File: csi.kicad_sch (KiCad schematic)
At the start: 0 parts

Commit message: finished v1
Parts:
- added J3: Conn_01x20, symbol Connector_Generic:Conn_01x20
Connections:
- new net +3.3V: J3.8 (Pin_8)
- new net CSI_DATA_2: J3.11 (Pin_11)
- new net CSI_DATA_3: J3.18 (Pin_18)
- new net CSI_DATA_4: J3.14 (Pin_14)
- new net CSI_DATA_5: J3.16 (Pin_16)
- new net CSI_DATA_6: J3.9 (Pin_9)
- new net CSI_DATA_7: J3.13 (Pin_13)
- new net CSI_DATA_8: J3.10 (Pin_10)
- new net CSI_DATA_9: J3.12 (Pin_12)
- new net CSI_HSYNC: J3.15 (Pin_15)
- new net CSI_MCLK: J3.1 (Pin_1)
- new net CSI_PIXCLK: J3.20 (Pin_20)
- new net CSI_VSYNC: J3.17 (Pin_17)
- new net GND: J3.19 (Pin_19), J3.2 (Pin_2)
- new net LDO_EN: J3.7 (Pin_7)
- new net LPI2C2_SCL: J3.4 (Pin_4)
- new net LPI2C2_SDA: J3.3 (Pin_3)
- new net PWDN: J3.6 (Pin_6)
- new net XRS: J3.5 (Pin_5)
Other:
- note added: "????"
- company: (none) -> Northeastern University
- title: (none) -> RT1050 DevBoard for Project Horizon

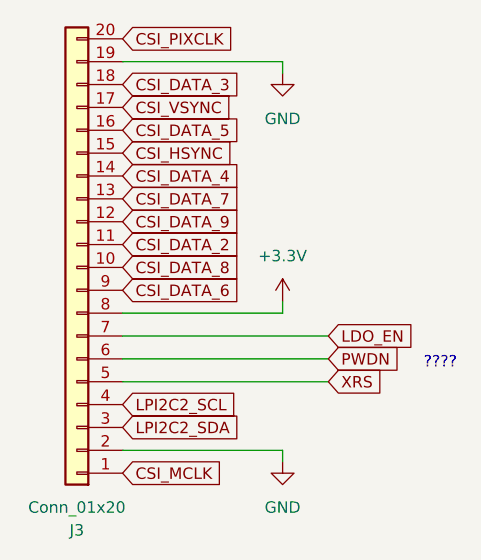
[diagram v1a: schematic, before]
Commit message: added load switches
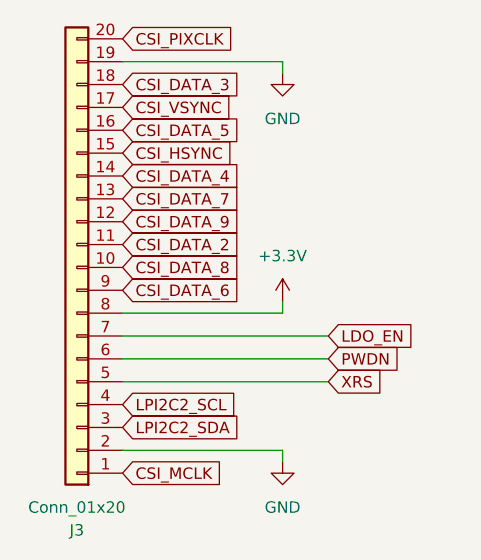
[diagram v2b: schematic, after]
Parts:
- J3: footprint (none) -> Connector_FFC-FPC:Molex_200528-0200_1x20-1MP_P1.00mm_Horizontal
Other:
- note removed: "????"
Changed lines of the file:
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@@
-		)
-	)
-	(text "????\n"
-		(exclude_from_sim no)
-		(at 72.136 65.278 0)
-		(effects
-			(font
-				(size 1.27 1.27)
-			)
 		)
 	)
@@
 			)
 		)
-		(property "Footprint" ""
+		(property "Footprint" "Connector_FFC-FPC:Molex_200528-0200_1x20-1MP_P1.00mm_Horizontal"
 			(at 31.75 54.61 0)
 			(effects
